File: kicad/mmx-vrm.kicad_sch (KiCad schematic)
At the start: 29 parts, among them J1 Conn_02x15_Row_Letter_First, Q1 Q_NMOS_GDS, Q2 Q_NMOS_GDS, Q3 Q_NPN_BEC, SW1 SW_DIP_x04, U1 NCP1579

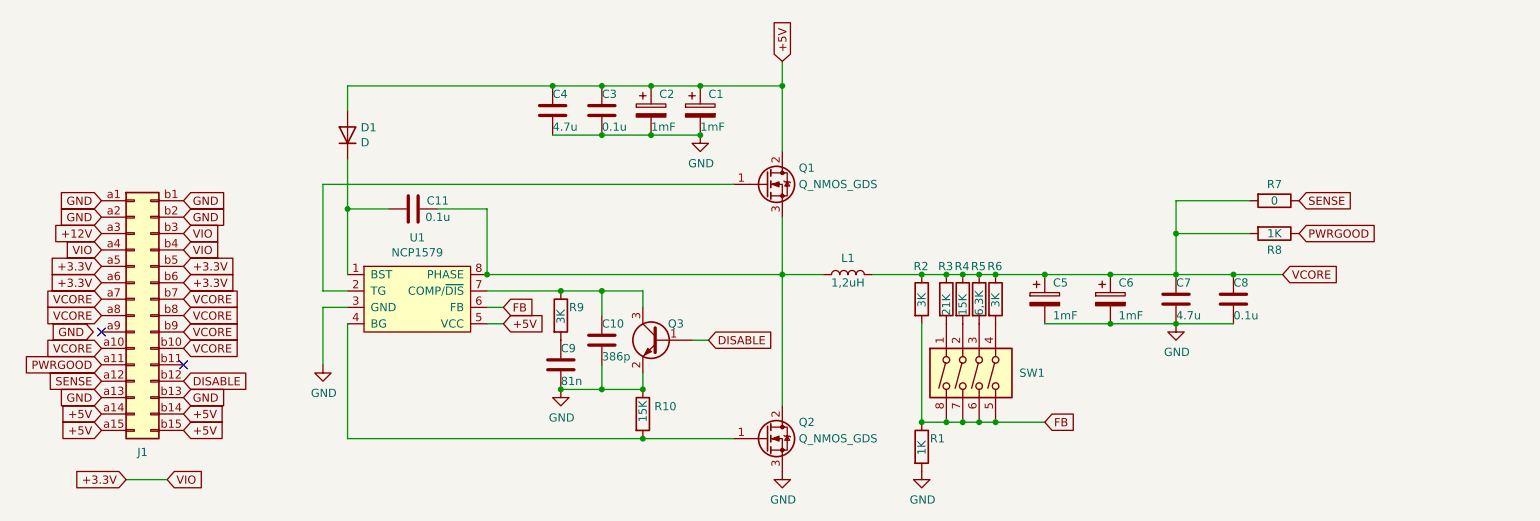
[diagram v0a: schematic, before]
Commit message: Wide version
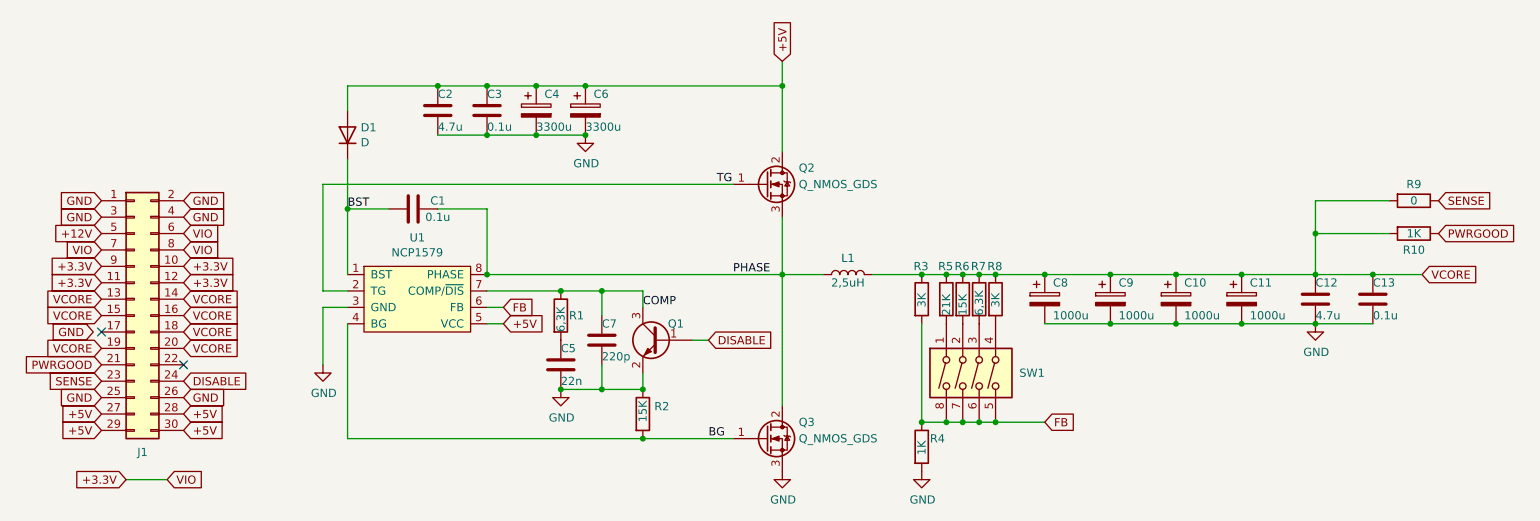
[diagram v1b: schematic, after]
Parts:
- removed C1: 1mF, Capacitor_THT:CP_Radial_D6.3mm_P2.50mm, symbol Device:CP
- added C10, C11: 1000u, Capacitor_THT:CP_Radial_D8.0mm_P3.50mm, symbol Device:CP
- added C6: 3300u, Capacitor_THT:CP_Radial_D10.0mm_P5.00mm, symbol Device:CP
- C4: renamed from C2; value 1mF -> 3300u; footprint Capacitor_THT:CP_Radial_D6.3mm_P2.50mm -> Capacitor_THT:CP_Radial_D10.0mm_P5.00mm; LCSC C494544 -> C407862
- C5: renamed from C9; value 81n -> 22n; LCSC C976248 -> C282848
- C7: renamed from C10; value 386p -> 220p; LCSC C2760364 -> C377077
- C8: renamed from C5; value 1mF -> 1000u; footprint Capacitor_THT:CP_Radial_D6.3mm_P2.50mm -> Capacitor_THT:CP_Radial_D8.0mm_P3.50mm; LCSC C494544 -> C407858
- C9: renamed from C6; value 1mF -> 1000u; footprint Capacitor_THT:CP_Radial_D6.3mm_P2.50mm -> Capacitor_THT:CP_Radial_D8.0mm_P3.50mm; LCSC C494544 -> C407858
- J1: footprint mmx-vrm:EDGE_30-pin -> Connector_PinSocket_2.54mm:PinSocket_2x15_P2.54mm_Horizontal; symbol Connector_Generic:Conn_02x15_Row_Letter_First -> Connector_Generic:Conn_02x15_Odd_Even; LCSC C132129 -> C2897435
- L1: value 1,2uH -> 2,5uH; footprint Inductor_SMD:L_12x12mm_H4.5mm -> Inductor_THT:L_Toroid_Vertical_L16.0mm_W8.0mm_P7.62mm; LCSC C337553 -> (none)
- R1: renamed from R9; value 3K -> 6,3K; LCSC C229609 -> C229767
- renumbered C11 to C1, C7 to C12, C8 to C13, C4 to C2, Q3 to Q1, Q1 to Q2, Q2 to Q3, R8 to R10, R10 to R2, R2 to R3, R1 to R4, R3 to R5, R4 to R6, R5 to R7, R6 to R8, R7 to R9
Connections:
- net +12V: now also J1.5 (Pin_5); no longer J1.a3 (Pin_a3)
- net +3.3V: now also J1.10 (Pin_10), J1.11 (Pin_11), J1.12 (Pin_12), J1.6 (Pin_6), J1.7 (Pin_7), J1.8 (Pin_8), J1.9 (Pin_9); no longer J1.a4 (Pin_a4), J1.a5 (Pin_a5), J1.a6 (Pin_a6), J1.b3 (Pin_b3), J1.b4 (Pin_b4), J1.b5 (Pin_b5), J1.b6 (Pin_b6)
- net +5V: now also J1.27 (Pin_27), J1.28 (Pin_28), J1.29 (Pin_29), J1.30 (Pin_30), C6.1; no longer J1.a14 (Pin_a14), J1.a15 (Pin_a15), J1.b14 (Pin_b14), J1.b15 (Pin_b15)
- net DISABLE: now also J1.24 (Pin_24); no longer J1.b12 (Pin_b12)
- net GND: now also J1.1 (Pin_1), J1.2 (Pin_2), J1.25 (Pin_25), J1.26 (Pin_26), J1.3 (Pin_3), J1.4 (Pin_4), C10.2, C11.2, C6.2; no longer J1.a1 (Pin_a1), J1.a13 (Pin_a13), J1.a2 (Pin_a2), J1.b1 (Pin_b1), J1.b13 (Pin_b13), J1.b2 (Pin_b2)
- net PWRGOOD: now also J1.21 (Pin_21); no longer J1.a11 (Pin_a11)
- net SENSE: now also J1.23 (Pin_23); no longer J1.a12 (Pin_a12)
- net VCORE: now also J1.13 (Pin_13), J1.14 (Pin_14), J1.15 (Pin_15), J1.16 (Pin_16), J1.18 (Pin_18), J1.19 (Pin_19), J1.20 (Pin_20), C10.1, C11.1; no longer J1.a10 (Pin_a10), J1.a7 (Pin_a7), J1.a8 (Pin_a8), J1.b10 (Pin_b10), J1.b7 (Pin_b7), J1.b8 (Pin_b8), J1.b9 (Pin_b9)
- net PHASE: now reaches C1.2, L1.1, Q2.3 (S), Q3.2 (D), U1.8 (PHASE)
- net BST: now reaches C1.1, D1.1 (K), U1.1 (BST)
- net TG: now reaches Q2.1 (G), U1.2 (TG)
- net BG: now reaches Q3.1 (G), R2.2, U1.4 (BG)
- net COMP: now reaches C7.1, Q1.3 (C), R1.1, U1.7 (COMP/~{DIS})
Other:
- moved on the sheet: C12, C13, C2, C3, C4, R10, R9

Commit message: Updated parameters
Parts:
- R1: value 6,3K -> 15K
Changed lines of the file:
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@@
       (effects (font (size 1.27 1.27)) (justify left))
     )
-    (property "Value" "6,3K" (at 134.62 106.68 90)
+    (property "Value" "15K" (at 134.62 106.68 90)
       (effects (font (size 1.27 1.27)) (justify left))
     )
